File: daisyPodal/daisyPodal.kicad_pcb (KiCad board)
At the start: 2 copper layers, 76 x 82 mm, 56 parts, among them J1 Guitar in, J2 fsw pin 1, J3 fsw pin 2, J4 fsw pin 4, J5 fsw pin 5, J6 fsw pin 6, J7 Left out, J8 Right out, J9 fsw pin 3, SW1 Switch 1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

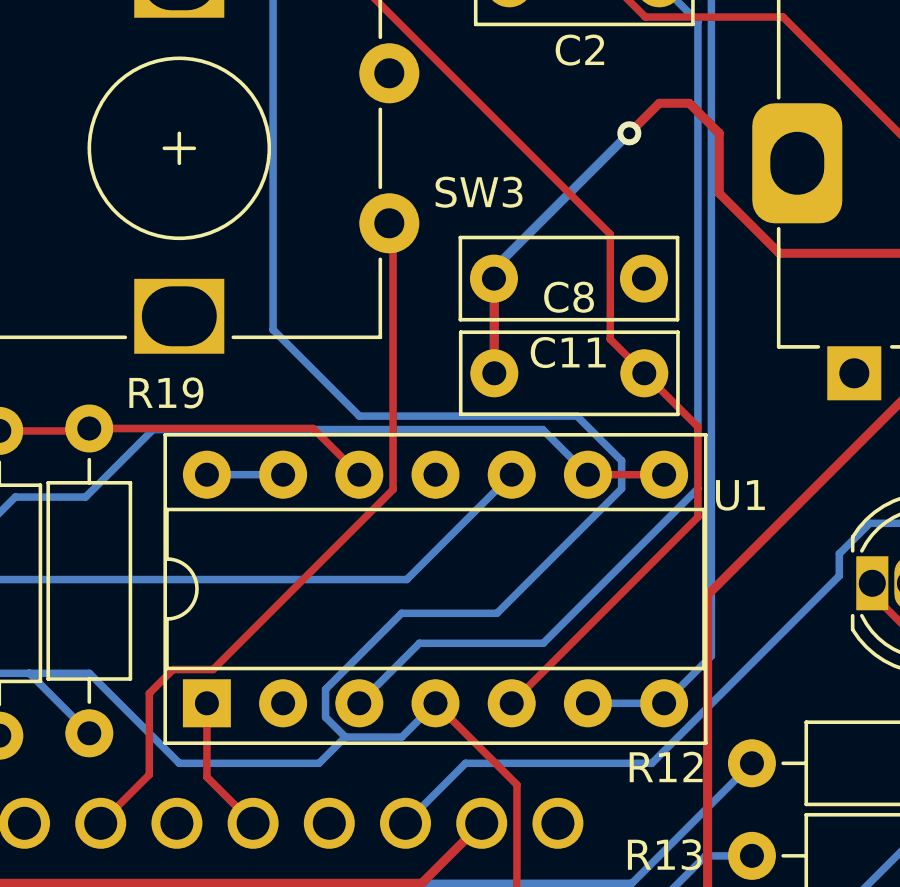
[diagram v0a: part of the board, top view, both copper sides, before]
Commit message: Fix missing connection in schematic on input stage
Means a jumper needed between pins 1 and 2 of TL074
on board v0.2
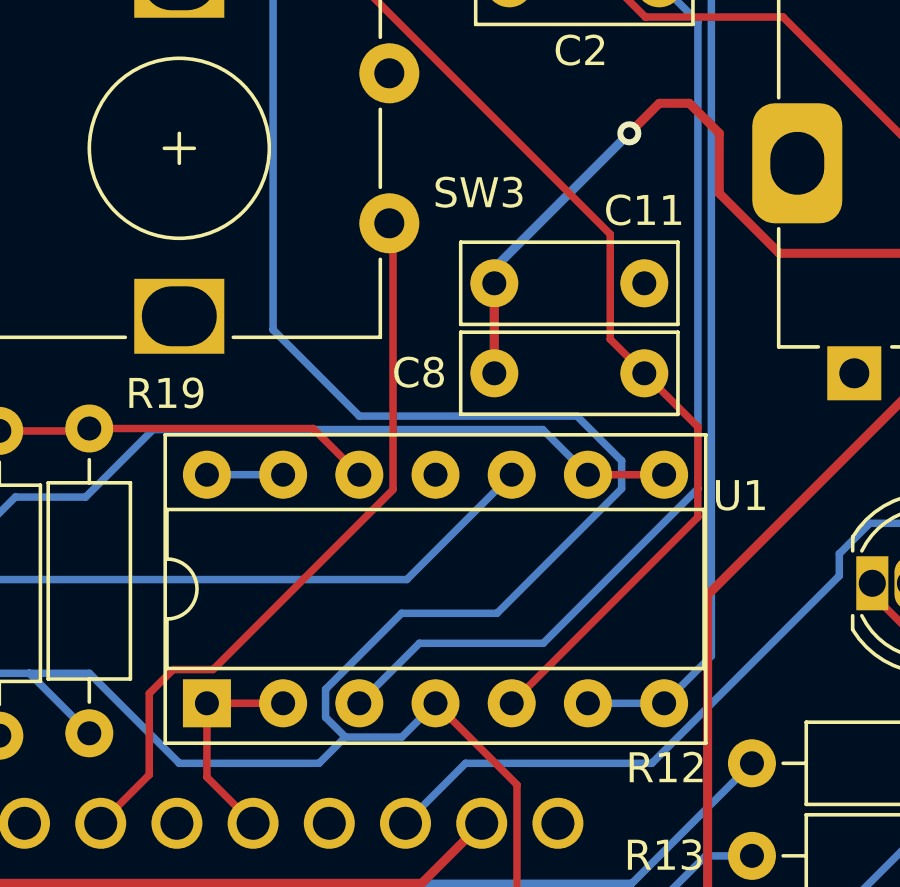
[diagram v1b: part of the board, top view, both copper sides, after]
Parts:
- moved C11 0.16 mm to (152.5, 92.0)
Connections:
- U1 pad 2: unconnected-(U1A---Pad2) -> /Left in
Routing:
- net /Left in: track 4.64 -> 7.18 mm
